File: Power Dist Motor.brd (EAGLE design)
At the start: 40.3 x 40.6 mm, 12 parts, among them IC1 LM350

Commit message: A bit more
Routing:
- net GND: track 0.00 -> 85.5 mm
- net N$1: track 0.00 -> 74.4 mm
- net N$7: track 0.00 -> 70.7 mm
- net N$2: track 0.00 -> 68.2 mm
- net N$4: track 0.00 -> 61.8 mm
- net N$3: track 0.00 -> 28.9 mm
- net N$5: track 0.00 -> 10.0 mm

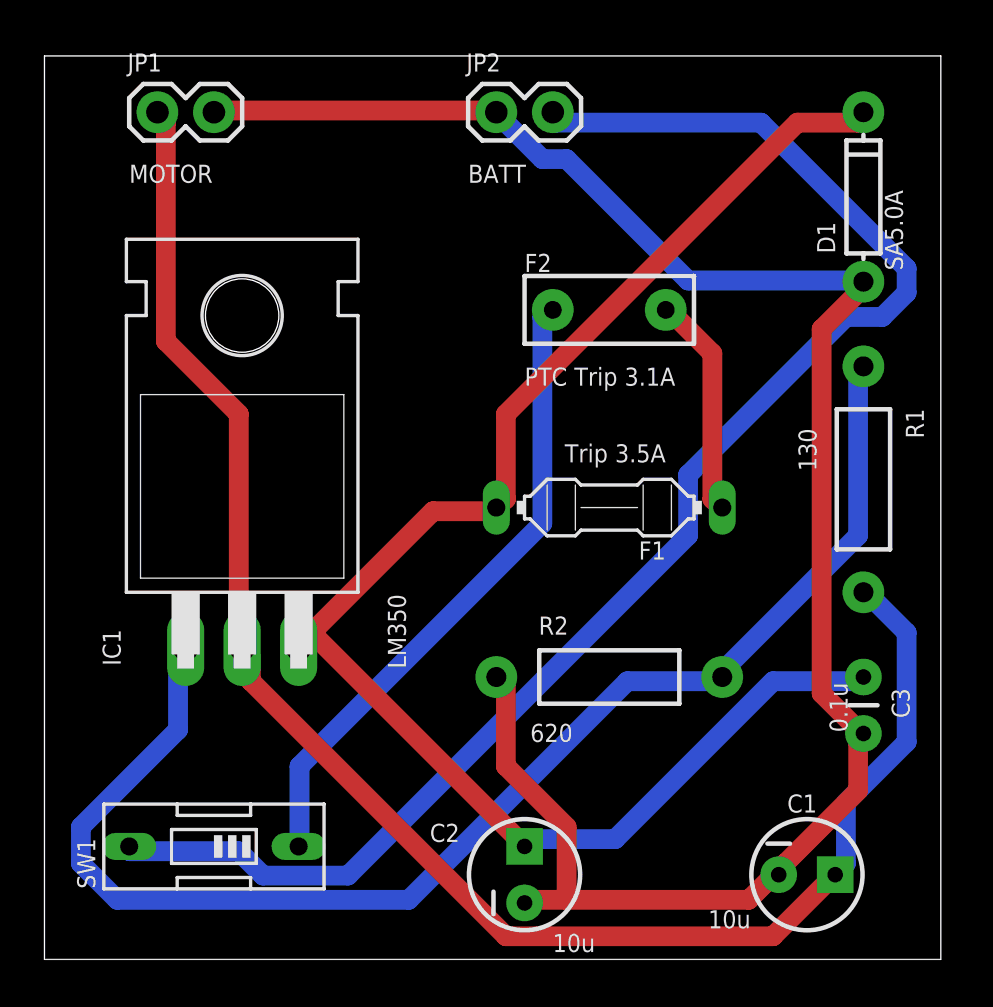
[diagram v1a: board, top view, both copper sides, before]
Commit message: fix outline
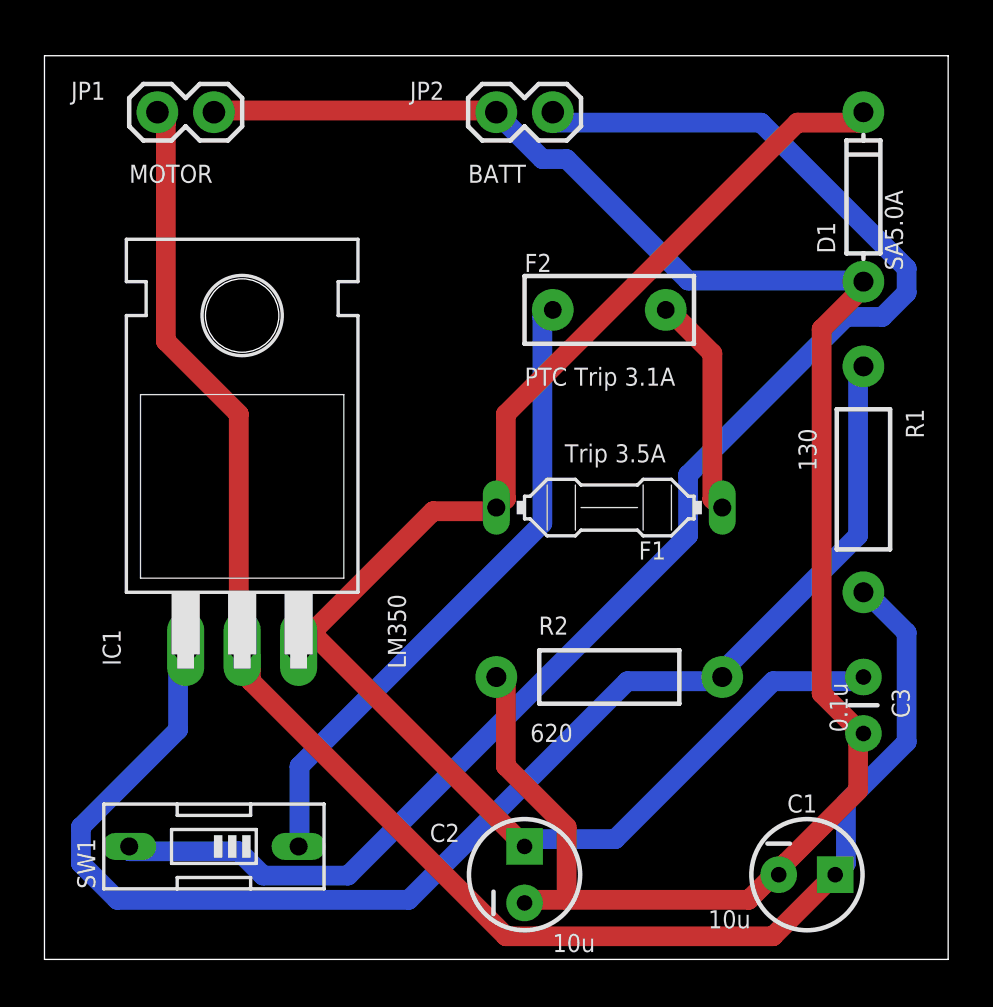
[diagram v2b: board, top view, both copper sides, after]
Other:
- board size 40.3 x 40.6 mm -> 40.6 x 40.6 mm
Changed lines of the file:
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@@
 <board>
 <plain>
-<wire x1="0" y1="39.37" x2="40.31" y2="39.37" width="0" layer="25"/>
-<wire x1="40.31" y1="39.37" x2="40.31" y2="80" width="0" layer="20"/>
-<wire x1="40.31" y1="80" x2="0" y2="80" width="0" layer="20"/>
-<wire x1="0" y1="80" x2="0" y2="39.37" width="0" layer="20"/>
+<wire x1="0" y1="80.01" x2="0" y2="39.37" width="0" layer="20"/>
+<wire x1="0" y1="39.37" x2="40.64" y2="39.37" width="0" layer="20"/>
+<wire x1="40.64" y1="39.37" x2="40.64" y2="80.01" width="0" layer="20"/>
+<wire x1="0" y1="80.01" x2="40.64" y2="80.01" width="0" layer="20"/>
 </plain>
 <attributes>
@@
 </element>
 <element name="JP1" library="SparkFun-Connectors" package="1X02" value="MOTOR" x="5.08" y="77.47" smashed="yes">
-<attribute name="NAME" x="3.7338" y="79.2988" size="0.8128" layer="25" ratio="10"/>
+<attribute name="NAME" x="1.1938" y="78.0288" size="0.8128" layer="25" ratio="10"/>
 <attribute name="VALUE" x="3.81" y="74.295" size="0.8128" layer="25"/>
 </element>
@@
 </element>
 <element name="JP2" library="SparkFun-Connectors" package="1X02" value="BATT" x="20.32" y="77.47" smashed="yes">
-<attribute name="NAME" x="18.9738" y="79.2988" size="0.8128" layer="25" ratio="10"/>
+<attribute name="NAME" x="16.4338" y="78.0288" size="0.8128" layer="25" ratio="10"/>
 <attribute name="VALUE" x="19.05" y="74.295" size="0.8128" layer="25"/>
 </element>
